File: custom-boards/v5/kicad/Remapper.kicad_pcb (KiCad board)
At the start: 2 copper layers, 27 x 100 mm, 67 parts, among them SW102 SW_Push, U1 SL2.1A, U103 RP2040, U105 W25Q128JVS, U3 RP2040, U4 TLV73333PDBV, U5 W25Q128JVS, Y1 Crystal_GND24, Y101 Crystal_GND24

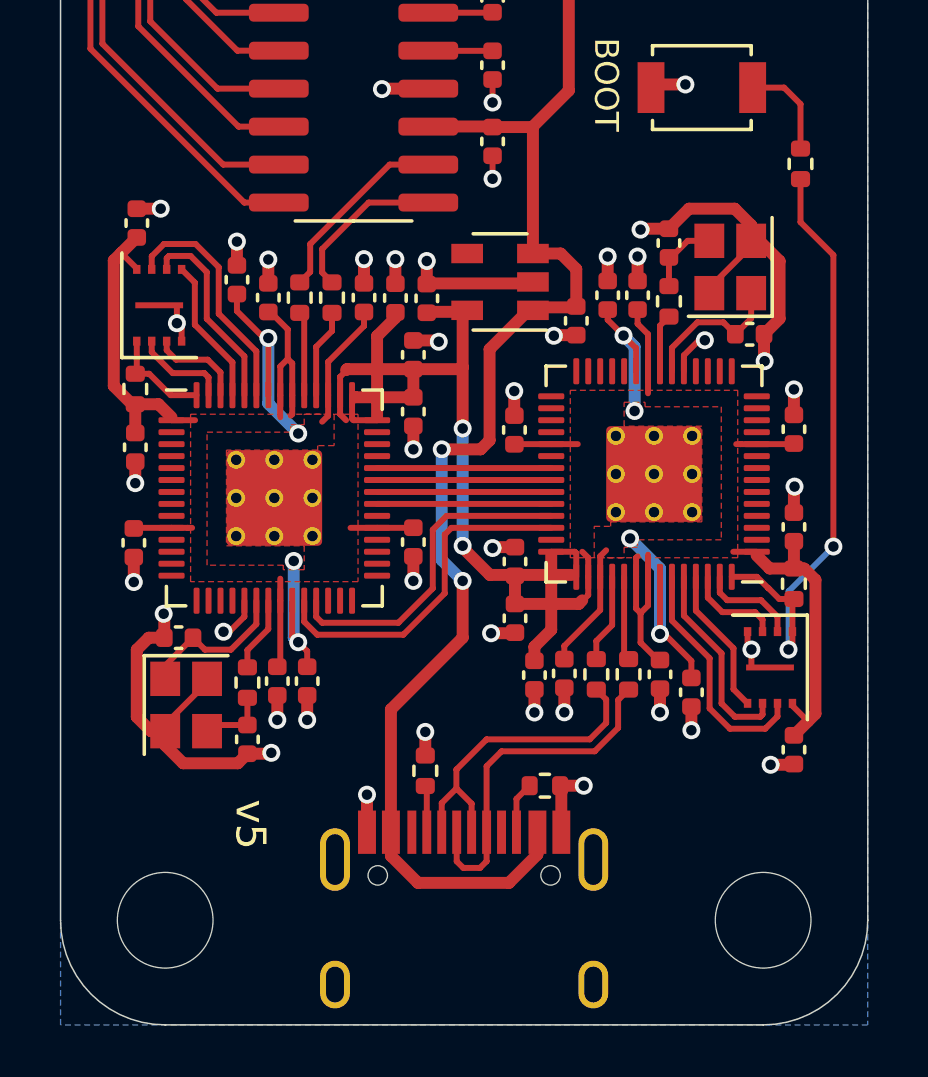
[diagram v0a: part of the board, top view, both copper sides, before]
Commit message: Update custom boards
This commit makes the following changes to the custom PCB designs.

v1-v5: flash chip footprint changed, previous one caused issues in
manufacturing. Some other components moved around as a result.

v1-v5: flash chip changed from 1 megabyte to 2 megabyte one.

v1: USB Type A port component changed, previous one was consistently
soldered on crooked by JLCPCB.

The new designs are named v1.1-v5.1.

Schematics and enclosure files are unchanged.
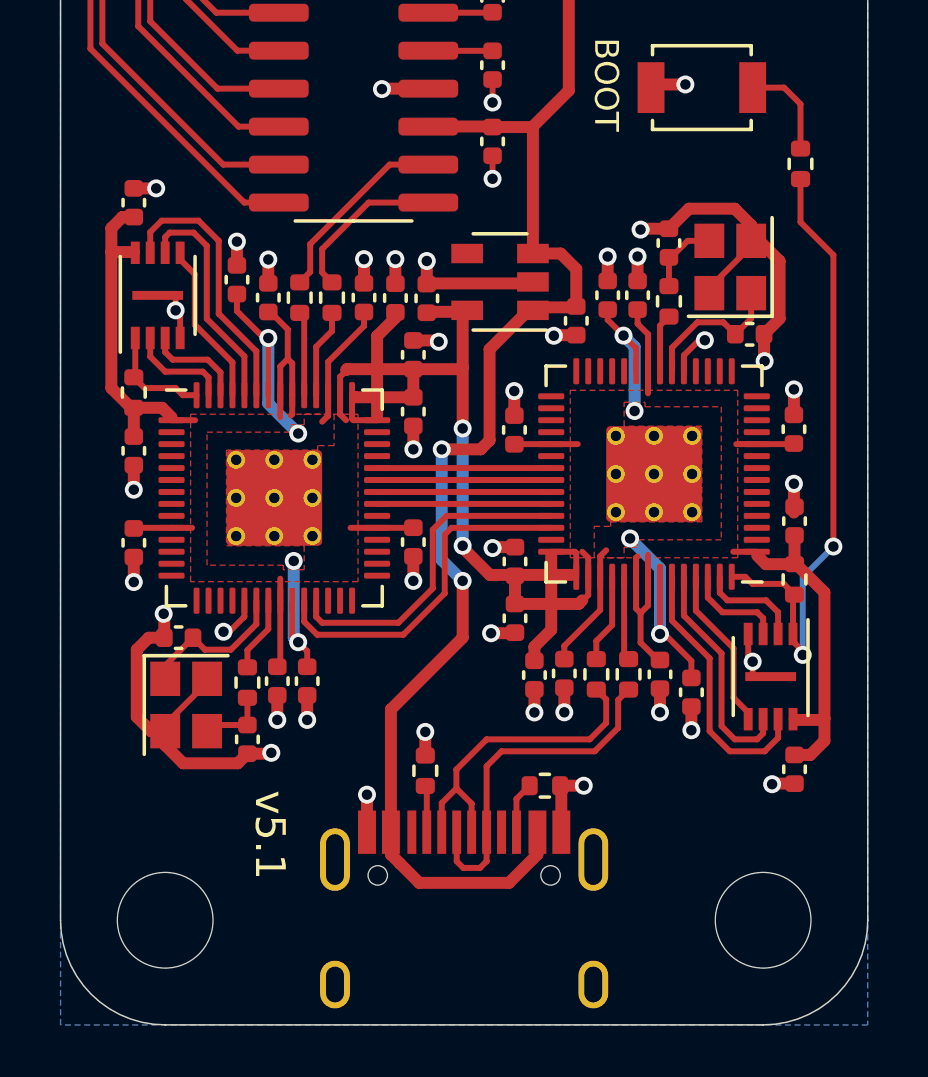
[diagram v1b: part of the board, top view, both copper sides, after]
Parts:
- moved C17 0.69 mm to (130.9, 88.5)
- moved C117 0.66 mm to (153.1, 107.5)
- moved U5 0.33 mm to (131.8, 91.6)
- moved U105 0.31 mm to (152.2, 104.3)
- moved C104 0.20 mm to (153.1, 99.2)
- moved R105 0.15 mm to (153.1, 101.1)
- moved C4 0.13 mm to (130.9, 96.8)
- moved R5 0.13 mm to (130.9, 94.8)
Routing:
- net +3V3: track 84.3 -> 86.7 mm
- net QSPI_SD3: track 7.97 -> 9.11 mm
- net QSPI_SCLK: track 6.61 -> 7.68 mm
- net 1QSPI_SD3: track 8.08 -> 9.07 mm
- net 1QSPI_SCLK: track 6.72 -> 7.65 mm
- net GND: track 67.7 -> 68.4 mm
- net QSPI_SD0: track 4.91 -> 5.49 mm
- net 1QSPI_SD0: track 4.95 -> 5.49 mm
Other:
- board text added: "v5.1"
- board text removed: "v5"
